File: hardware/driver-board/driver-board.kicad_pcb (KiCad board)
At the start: 4 copper layers, 111.8 x 83.8 mm, 69 parts, among them J1 Conn_ARM_JTAG_SWD_10, J2 USB_C_Receptacle_USB2.0_16P, J3 CONN_MOTOR_R, J4 CONN_MOTOR_L, Q1 AO3401A, Q2 AO4407A, SW1 SW_Push, SW2 SK-3296S-01-L2, U1 STM32F103CBT6, U2 USBLC6-2SC6, U3 DRV8838, U4 DRV8838, U5 LMR51430XDDCR, Y1 16Mhz

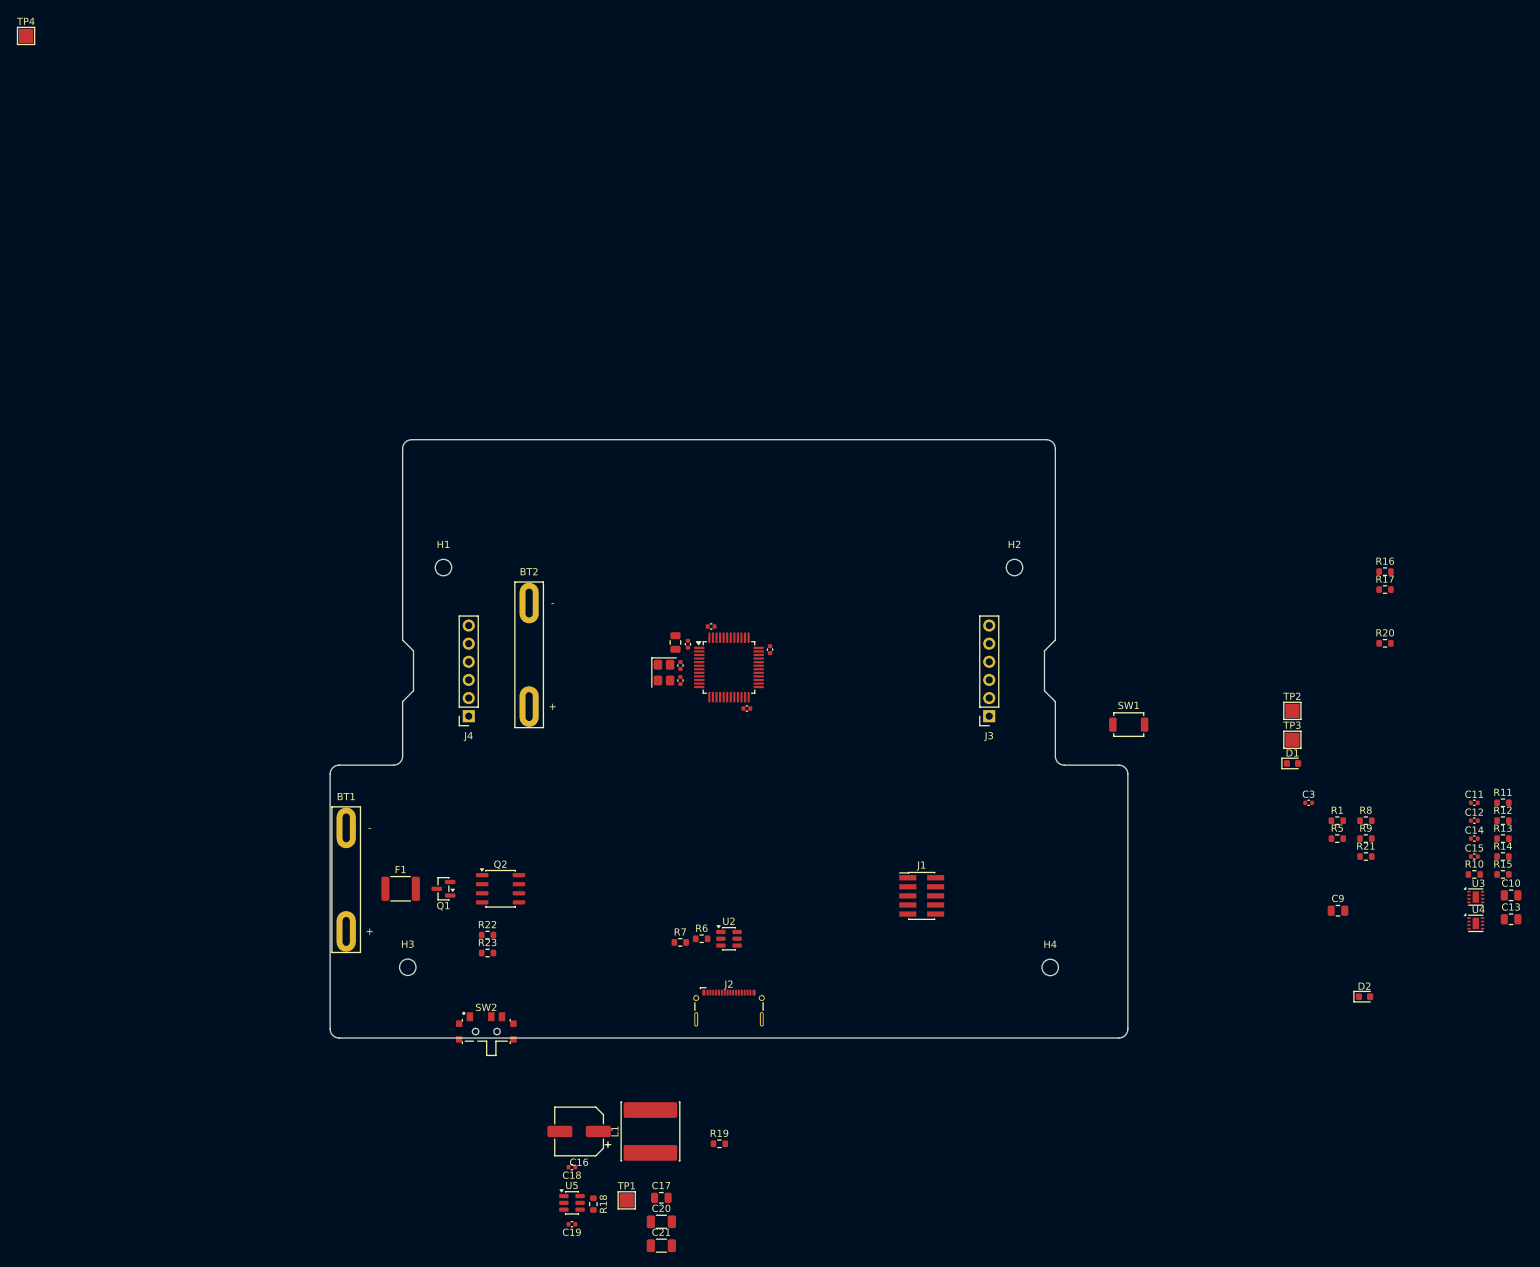
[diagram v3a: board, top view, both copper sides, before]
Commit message: Refine driver board placement and motor power checks
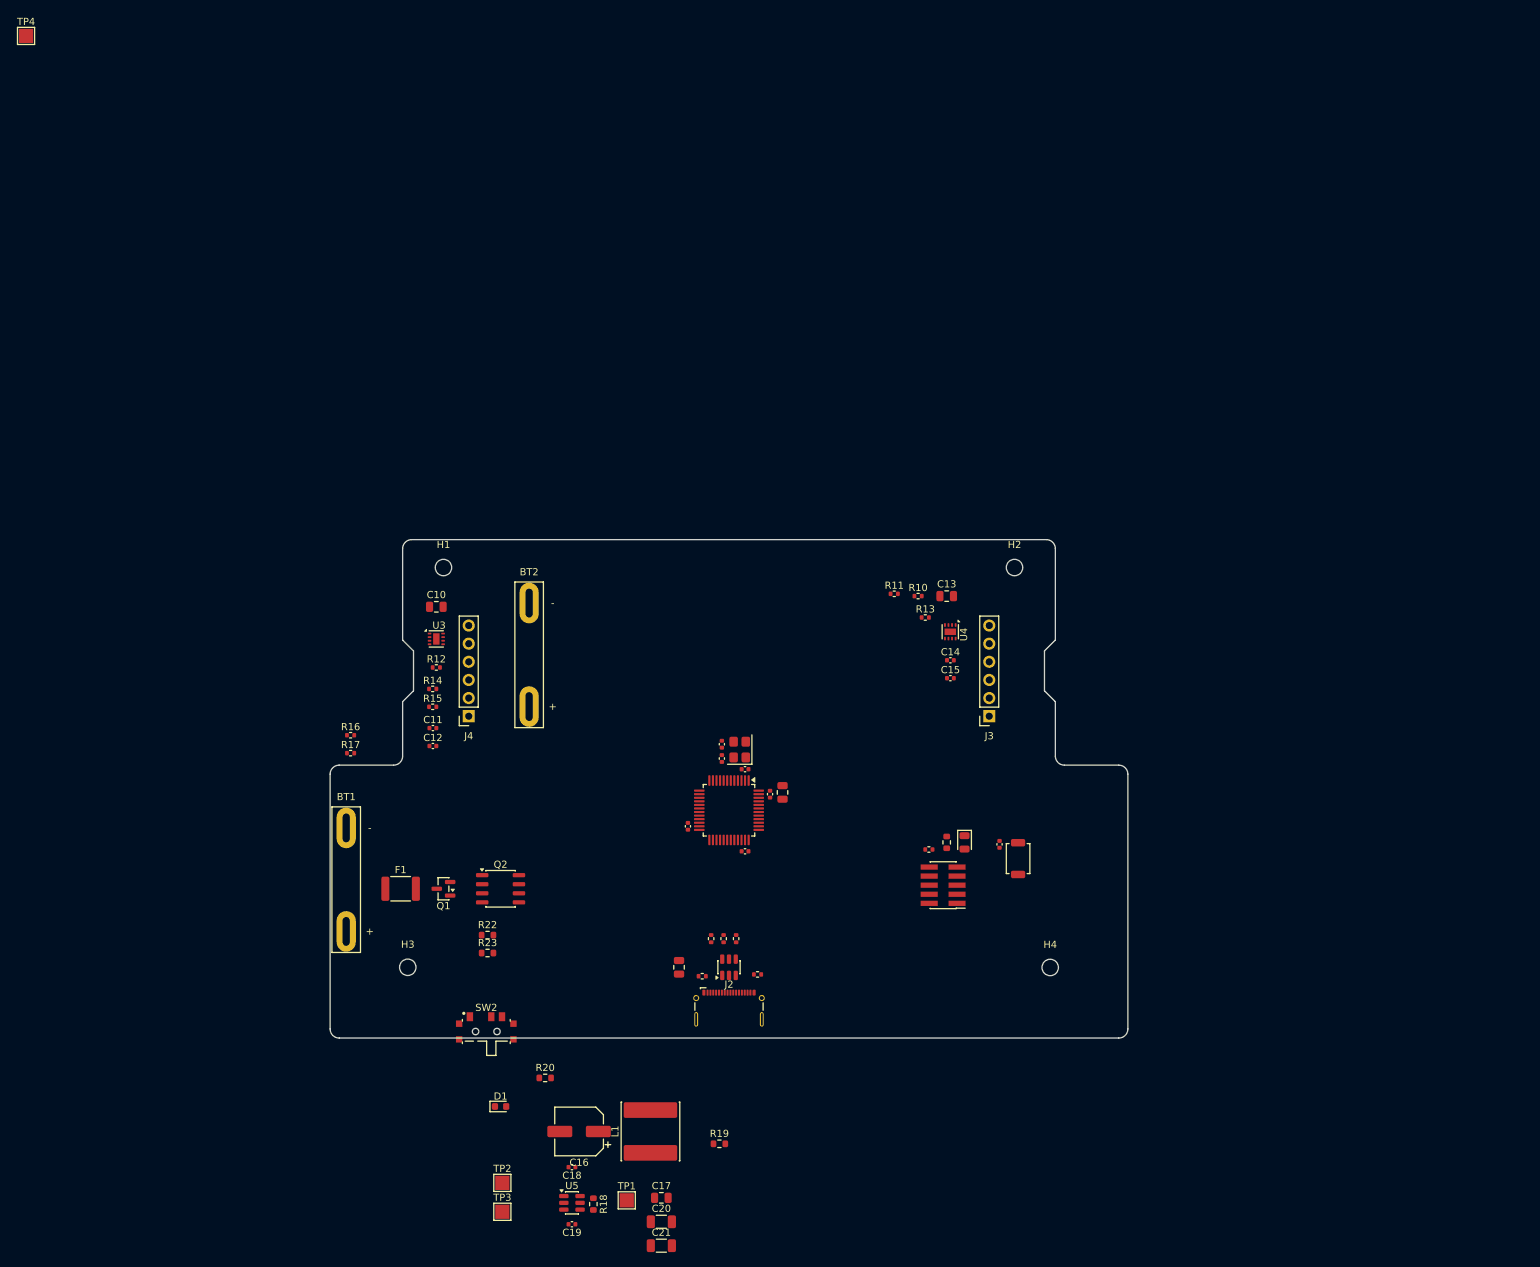
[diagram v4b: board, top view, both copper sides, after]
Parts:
- D2: footprint LED_SMD:LED_0603_1608Metric -> LED_SMD:LED_0805_2012Metric
- R1, R10, R11, R12, R13, R14, R15, R16, R17, R5, R6, R7, R8, R9: footprint Resistor_SMD:R_0603_1608Metric -> Resistor_SMD:R_0402_1005Metric
- moved C10 155.9 mm to (59.0, 81.5)
- moved R14 151.8 mm to (58.5, 93.0)
- moved R15 151.8 mm to (58.5, 95.5)
- moved R12 151.0 mm to (59.0, 90.0)
- moved U3 150.0 mm to (59.0, 86.0)
- moved R16 146.7 mm to (47.0, 99.5)
- moved R17 146.7 mm to (47.0, 102.0)
- moved C11 146.3 mm to (58.5, 98.5)
- moved C12 146.3 mm to (58.5, 101.0)
- moved R20 132.5 mm to (74.2, 147.5)
- moved TP2 128.9 mm to (68.2, 162.2)
- moved TP3 128.9 mm to (68.2, 166.2)
- moved D1 120.9 mm to (68.0, 151.5)
- moved C9 92.7 mm to (93.0, 132.0), turned to 90 degrees
- moved R8 91.5 mm to (99.2, 128.0), turned to -90 degrees
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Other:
- board size 111.8 x 83.8 mm -> 111.8 x 69.8 mm

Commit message: Refine switch footprint and board placement
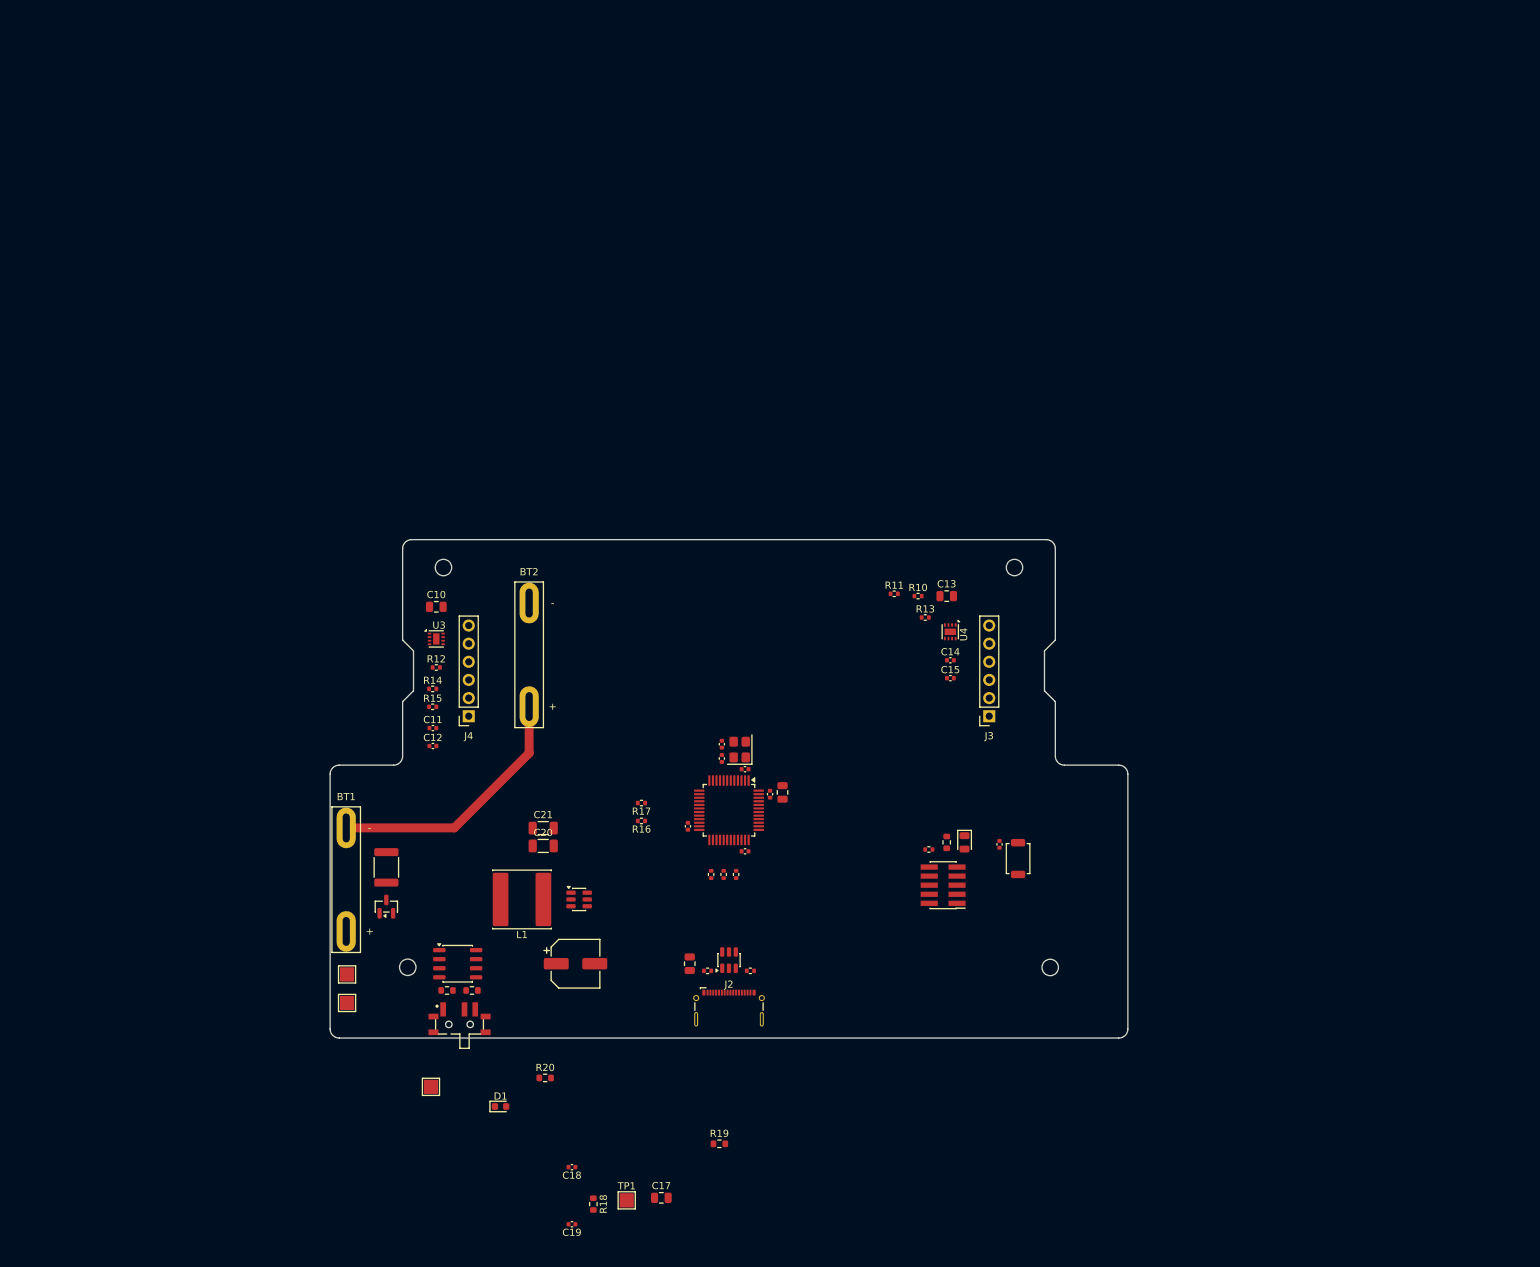
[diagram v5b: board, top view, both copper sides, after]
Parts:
- moved TP4 157.8 mm to (58.2, 148.8)
- moved C21 60.8 mm to (74.0, 112.5)
- moved C20 55.2 mm to (74.0, 115.0)
- moved U5 42.5 mm to (79.0, 122.5)
- moved R16 42.5 mm to (87.7, 111.5), turned to 180 degrees
- moved R17 41.3 mm to (87.7, 109.0), turned to 180 degrees
- moved TP3 39.7 mm to (46.5, 133.0)
- moved L1 37.2 mm to (71.0, 122.5), turned to 180 degrees
- moved TP2 33.3 mm to (46.5, 137.0)
- moved C16 23.5 mm to (78.5, 131.5), turned to 0 degrees
- moved Q2 12.1 mm to (62.0, 131.5)
- moved R22 9.61 mm to (60.5, 135.2), turned to 180 degrees
- moved R5 8.99 mm to (97.5, 119.0)
- moved R8 8.99 mm to (99.2, 119.0)
- moved R9 8.99 mm to (101.0, 119.0)
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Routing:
- net /Power/BT2+: track 0.00 -> 36.5 mm

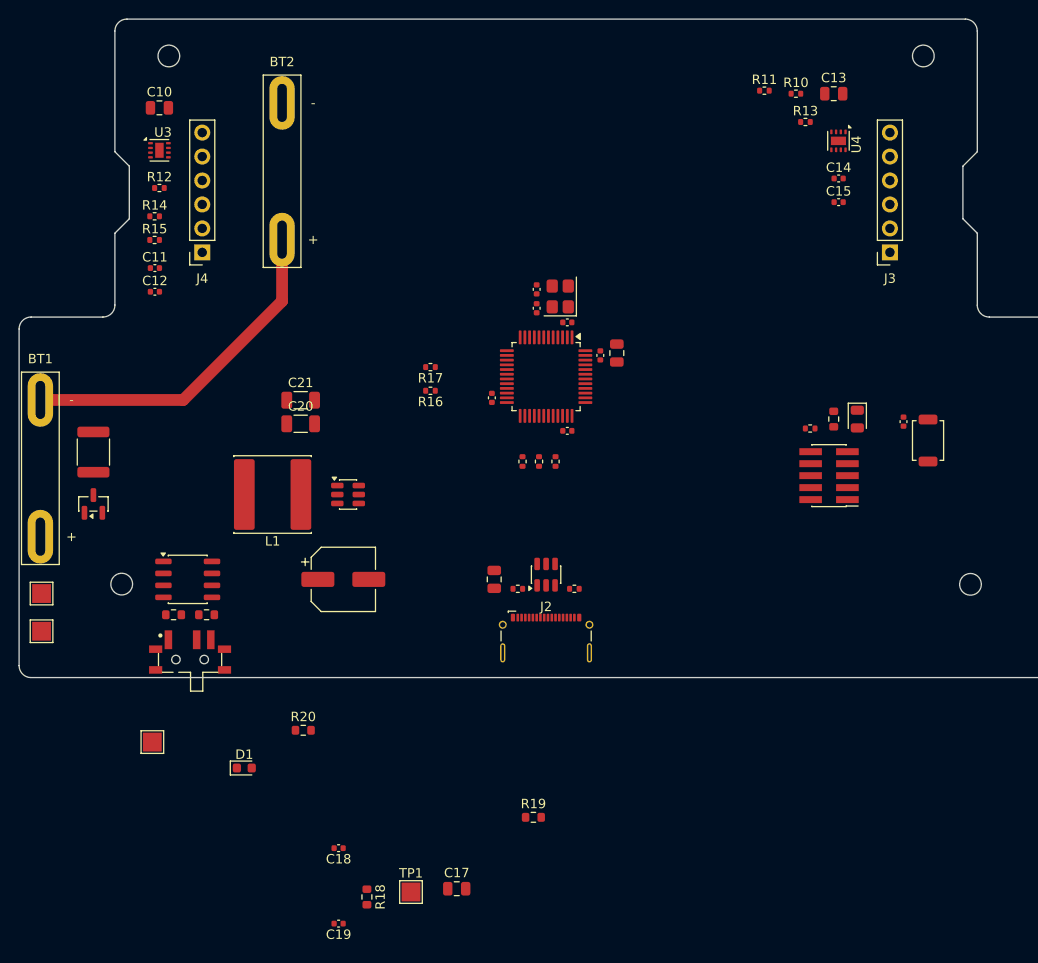
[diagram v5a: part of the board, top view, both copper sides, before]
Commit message: Refine Rev A PCB placement and decoupling
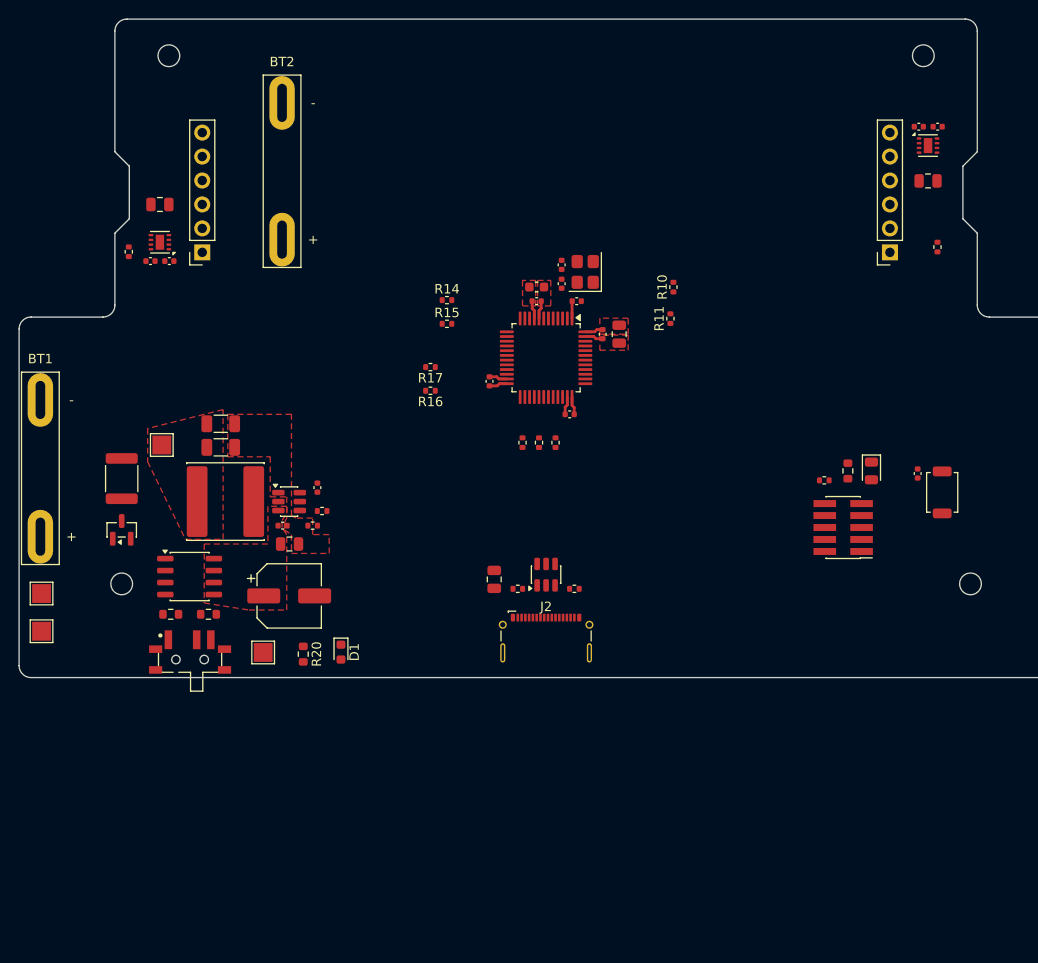
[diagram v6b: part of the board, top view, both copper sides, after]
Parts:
- added C22: 10n, Capacitor_SMD:C_0402_1005Metric, F.Cu at (99.0, 102.0)
- added C23: 1u, Capacitor_SMD:C_0603_1608Metric, F.Cu at (99.0, 100.5)
- R18, R19: footprint Resistor_SMD:R_0603_1608Metric -> Resistor_SMD:R_0402_1005Metric
- moved TP1 54.3 mm to (59.2, 117.2)
- moved C19 46.3 mm to (75.8, 121.8), turned to 90 degrees
- moved R18 41.2 mm to (76.2, 124.2), turned to 180 degrees
- moved C17 40.6 mm to (72.8, 127.8)
- moved R19 38.8 mm to (75.2, 125.8), turned to 180 degrees
- moved C18 34.7 mm to (72.1, 125.8), turned to 0 degrees
- moved R14 32.2 mm to (89.5, 101.9)
- moved R15 32.2 mm to (89.5, 104.4)
- moved R11 26.1 mm to (113.2, 103.8), turned to 90 degrees
- moved R10 24.3 mm to (113.5, 100.5), turned to 90 degrees
- moved R13 19.3 mm to (141.5, 96.3), turned to 90 degrees
- moved D1 16.0 mm to (78.2, 139.2), turned to -90 degrees
- moved TP4 15.1 mm to (70.0, 139.2)
- moved C13 13.6 mm to (140.5, 89.2)
- moved C15 13.2 mm to (141.5, 83.5)
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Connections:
- net Net-(U5-SW) renamed /Power/REG_SW
- J4 pad 1: /Motor Control/ML- -> /Motor Control/ML+
- J4 pad 2: /Motor Control/ML+ -> /Motor Control/ML-
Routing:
- net /Power/BT2+: track 36.5 -> 1.52 mm
- net +3V3: track 0.00 -> 9.58 mm
- net GND: track 0.00 -> 7.73 mm
- added copper zone on F.Cu, net +3V3
- added copper zone on F.Cu, net GND
- added copper zone on In1.Cu, net GND
- added copper zone on F.Cu, net VBAT_SW
